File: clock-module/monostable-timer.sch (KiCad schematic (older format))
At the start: 8 parts

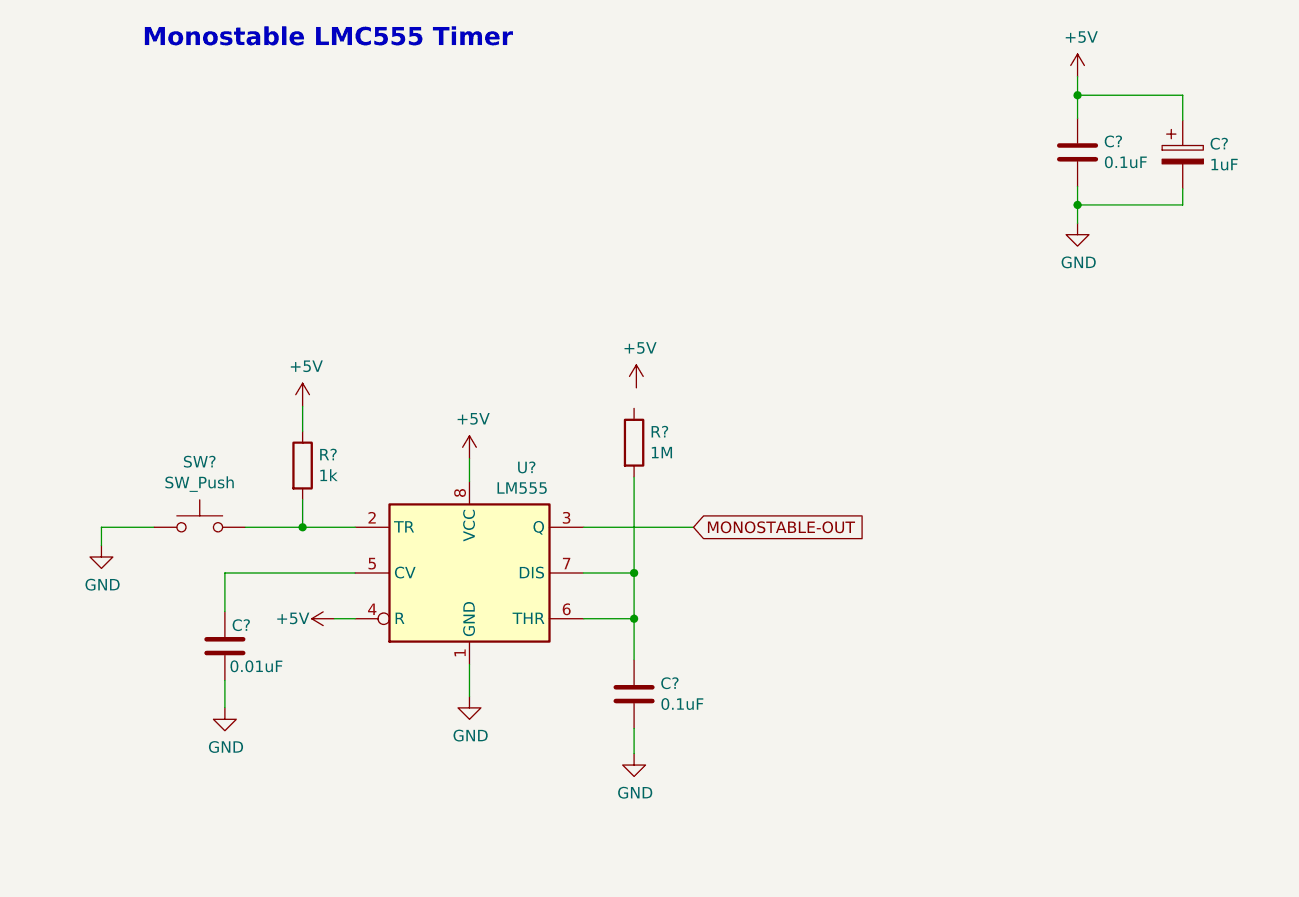
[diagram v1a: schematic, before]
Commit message: Add LED to all outputs of clocl-module
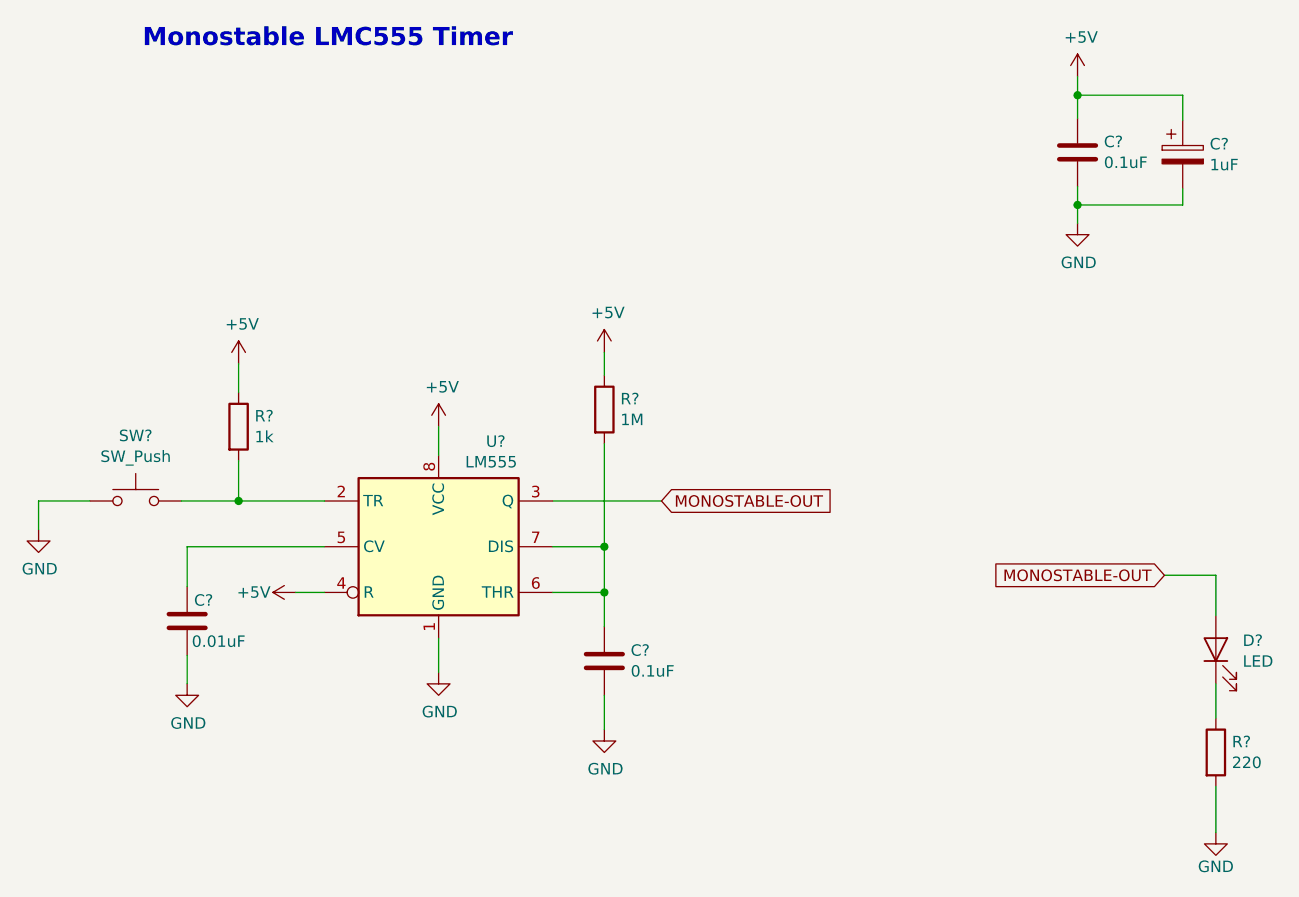
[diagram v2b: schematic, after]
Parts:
- added D?: LED, symbol Device:LED
- added R?: 220, symbol Device:R
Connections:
- net +5V: now also R?.1
- net GND: now also R?.2
- net MONOSTABLE-OUT: now also D?.2 (A)
- new net: D?.1 (K), R?.1
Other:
- moved on the sheet: C?, R?, SW?, U?

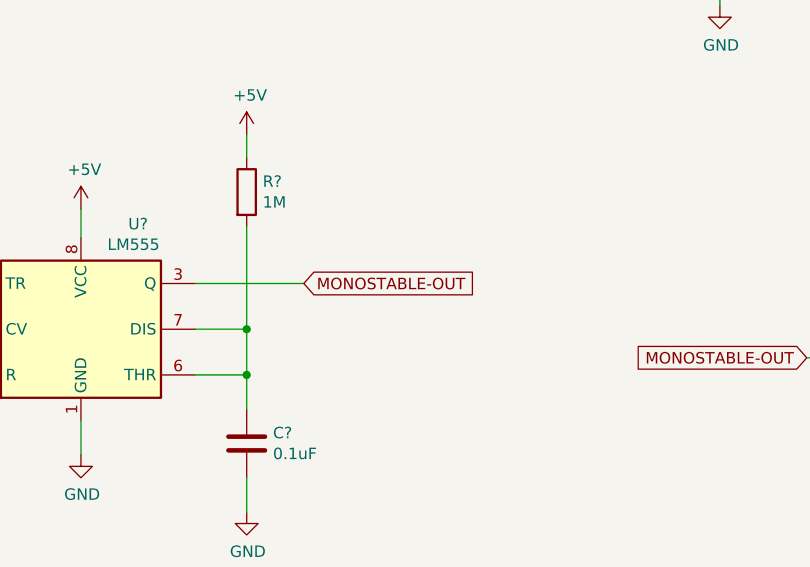
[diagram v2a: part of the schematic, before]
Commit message: Add clock inverter to clock-module, correct label directions
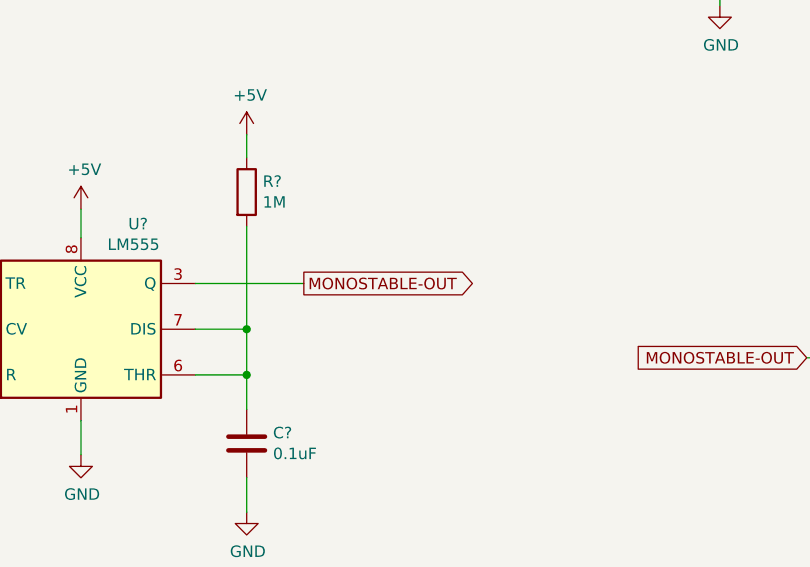
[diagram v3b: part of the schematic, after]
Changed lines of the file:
@@
 Wire Wire Line
 	9125 5075 9125 5275
-Text GLabel 6700 3825 2    50   Input ~ 0
+Text GLabel 6700 3825 2    50   Output ~ 0
 MONOSTABLE-OUT
 Wire Wire Line

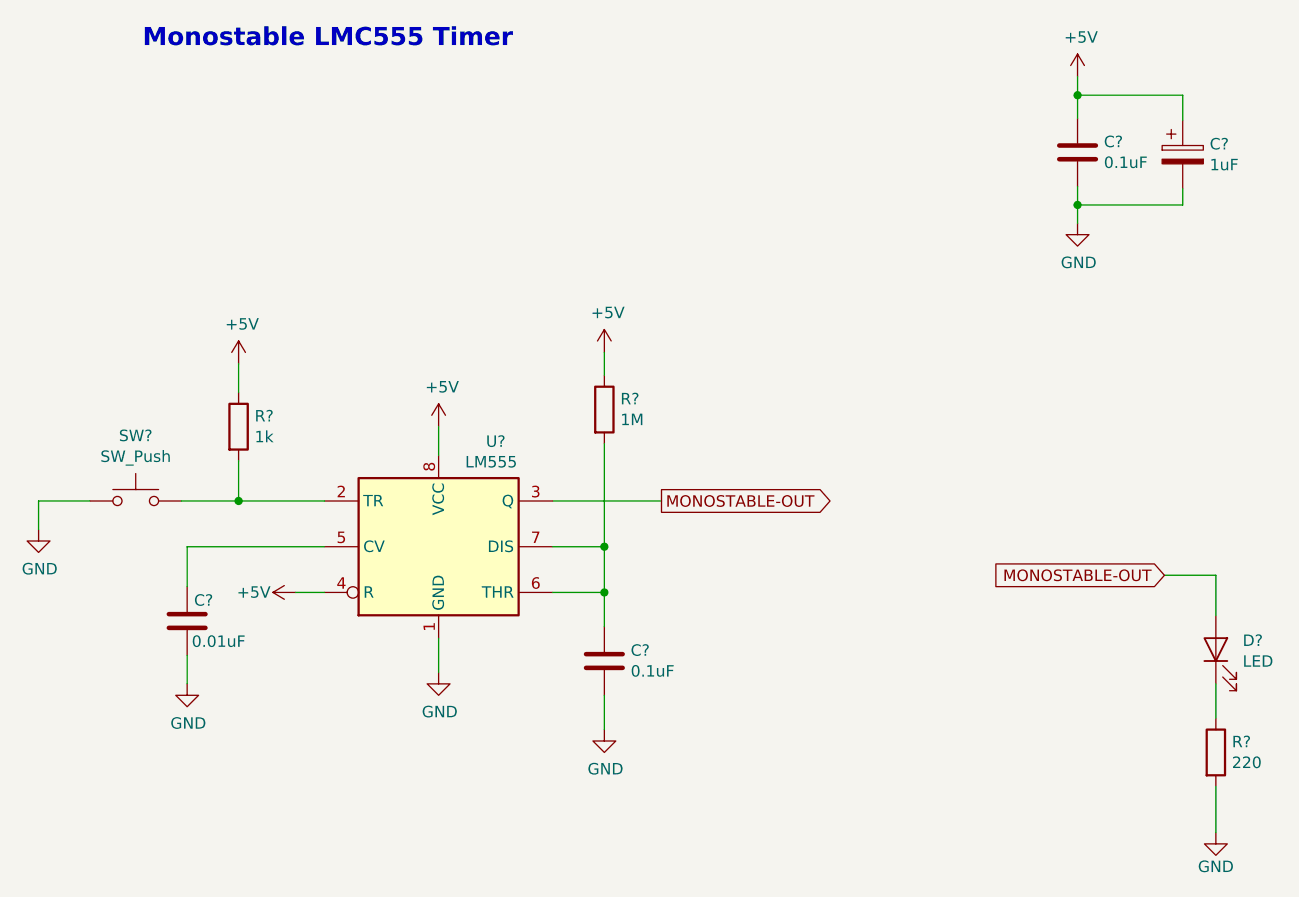
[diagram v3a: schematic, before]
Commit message: ERC complete on clock-module, add HLT connector
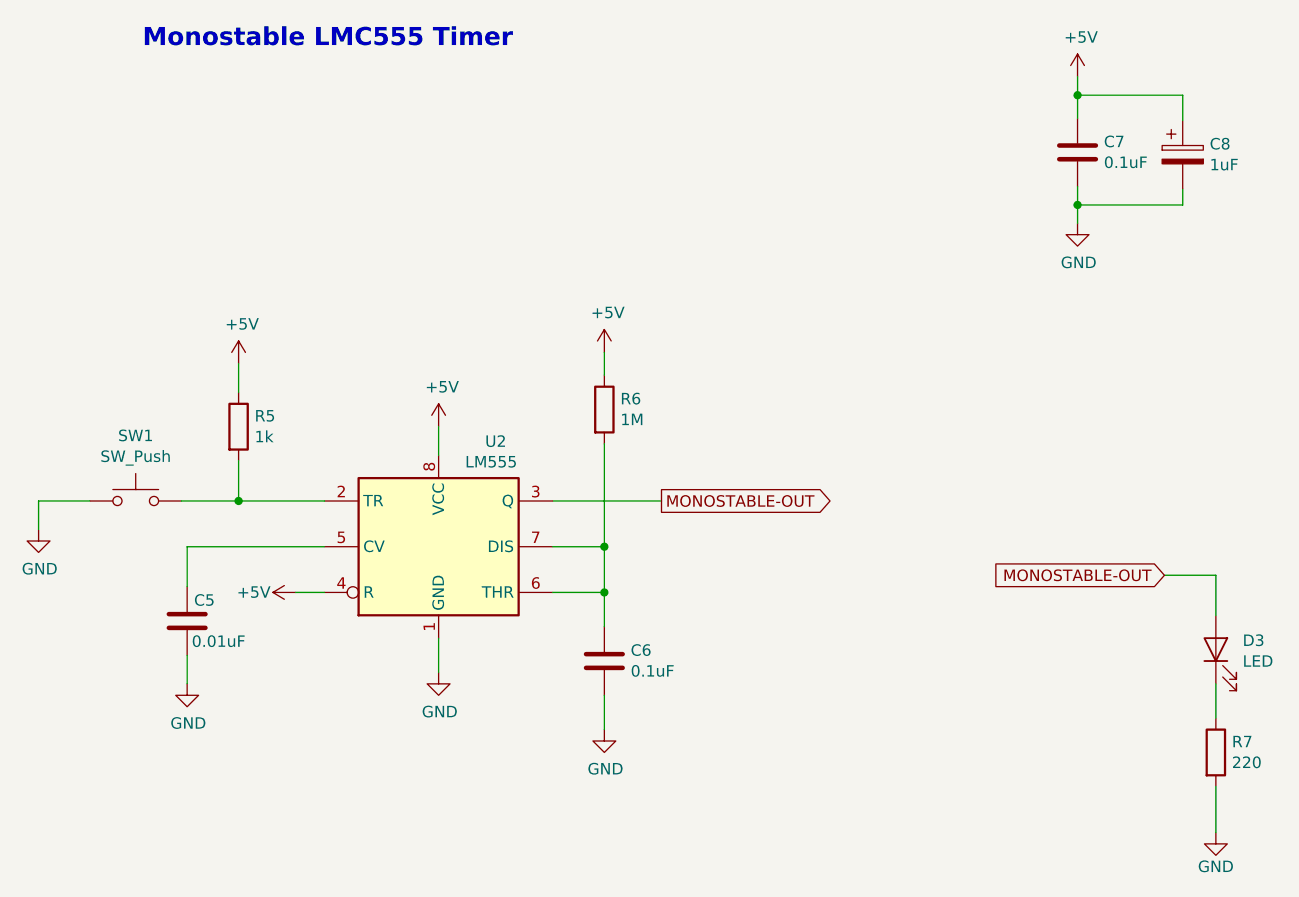
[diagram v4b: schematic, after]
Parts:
- gave numbers to parts that had none: 10
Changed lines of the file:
@@
 P 5725 4025
 AR Path="/5D27ED24" Ref="U?"  Part="1"
-AR Path="/5D26F003/5D27ED24" Ref="U?"  Part="1"
-F 0 "U?" H 5975 4485 50  0000 C CNN
+AR Path="/5D26F003/5D27ED24" Ref="U2"  Part="1"
+F 0 "U2" H 5975 4485 50  0000 C CNN
 F 1 "LM555" H 5955 4395 50  0000 C CNN
 F 2 "" H 5725 4025 50  0001 C CNN
@@
 P 4625 4350
 AR Path="/5D27ED2A" Ref="C?"  Part="1"
-AR Path="/5D26F003/5D27ED2A" Ref="C?"  Part="1"
-F 0 "C?" H 4655 4440 50  0000 L CNN
+AR Path="/5D26F003/5D27ED2A" Ref="C5"  Part="1"
+F 0 "C5" H 4655 4440 50  0000 L CNN
 F 1 "0.01uF" H 4645 4260 50  0000 L CNN
 F 2 "" H 4663 4200 50  0001 C CNN
@@
 P 8520 2300
 AR Path="/5D27ED30" Ref="C?"  Part="1"
-AR Path="/5D26F003/5D27ED30" Ref="C?"  Part="1"
-F 0 "C?" H 8635 2346 50  0000 L CNN
+AR Path="/5D26F003/5D27ED30" Ref="C7"  Part="1"
+F 0 "C7" H 8635 2346 50  0000 L CNN
 F 1 "0.1uF" H 8635 2255 50  0000 L CNN
 F 2 "" H 8558 2150 50  0001 C CNN
@@
 P 4850 3500
 AR Path="/5D27ED36" Ref="R?"  Part="1"
-AR Path="/5D26F003/5D27ED36" Ref="R?"  Part="1"
-F 0 "R?" H 4920 3546 50  0000 L CNN
+AR Path="/5D26F003/5D27ED36" Ref="R5"  Part="1"
+F 0 "R5" H 4920 3546 50  0000 L CNN
 F 1 "1k" H 4920 3455 50  0000 L CNN
 F 2 "" V 4780 3500 50  0001 C CNN
@@
 P 6450 3425
 AR Path="/5D27ED3C" Ref="R?"  Part="1"
-AR Path="/5D26F003/5D27ED3C" Ref="R?"  Part="1"
-F 0 "R?" H 6520 3471 50  0000 L CNN
+AR Path="/5D26F003/5D27ED3C" Ref="R6"  Part="1"
+F 0 "R6" H 6520 3471 50  0000 L CNN
 F 1 "1M" H 6520 3380 50  0000 L CNN
 F 2 "" V 6380 3425 50  0001 C CNN
@@
 P 4400 3825
 AR Path="/5D27ED42" Ref="SW?"  Part="1"
-AR Path="/5D26F003/5D27ED42" Ref="SW?"  Part="1"
-F 0 "SW?" H 4400 4110 50  0000 C CNN
+AR Path="/5D26F003/5D27ED42" Ref="SW1"  Part="1"
+F 0 "SW1" H 4400 4110 50  0000 C CNN
 F 1 "SW_Push" H 4400 4019 50  0000 C CNN
 F 2 "" H 4400 4025 50  0001 C CNN
@@
 Monostable LMC555 Timer
 $Comp
-L Device:CP C?
+L Device:CP C8
 U 1 1 5D27EF7E
 P 8980 2310
-F 0 "C?" H 9098 2356 50  0000 L CNN
+F 0 "C8" H 9098 2356 50  0000 L CNN
 F 1 "1uF" H 9098 2265 50  0000 L CNN
 F 2 "" H 9018 2160 50  0001 C CNN
@@
 $EndComp
 $Comp
-L power:+5V #PWR?
+L power:+5V #PWR0117
 U 1 1 5D284C5B
 P 8520 1970
-F 0 "#PWR?" H 8520 1820 50  0001 C CNN
+F 0 "#PWR0117" H 8520 1820 50  0001 C CNN
 F 1 "+5V" H 8535 2143 50  0000 C CNN
 F 2 "" H 8520 1970 50  0001 C CNN
@@
 P 6450 4525
 AR Path="/5D28683E" Ref="C?"  Part="1"
-AR Path="/5D26F003/5D28683E" Ref="C?"  Part="1"
-F 0 "C?" H 6565 4571 50  0000 L CNN
+AR Path="/5D26F003/5D28683E" Ref="C6"  Part="1"
+F 0 "C6" H 6565 4571 50  0000 L CNN
 F 1 "0.1uF" H 6565 4480 50  0000 L CNN
 F 2 "" H 6488 4375 50  0001 C CNN
@@
 $EndComp
 $Comp
-L power:+5V #PWR?
+L power:+5V #PWR0118
 U 1 1 5D28722A
 P 5725 3500
-F 0 "#PWR?" H 5725 3350 50  0001 C CNN
+F 0 "#PWR0118" H 5725 3350 50  0001 C CNN
 F 1 "+5V" H 5740 3673 50  0000 C CNN
 F 2 "" H 5725 3500 50  0001 C CNN
@@
 $EndComp
 $Comp
-L power:+5V #PWR?
+L power:+5V #PWR0119
 U 1 1 5D287ACE
 P 6450 3175
-F 0 "#PWR?" H 6450 3025 50  0001 C CNN
+F 0 "#PWR0119" H 6450 3025 50  0001 C CNN
 F 1 "+5V" H 6465 3348 50  0000 C CNN
 F 2 "" H 6450 3175 50  0001 C CNN
@@
 $EndComp
 $Comp
-L power:+5V #PWR?
+L power:+5V #PWR0120
 U 1 1 5D28807D
 P 5100 4225
-F 0 "#PWR?" H 5100 4075 50  0001 C CNN
+F 0 "#PWR0120" H 5100 4075 50  0001 C CNN
 F 1 "+5V" V 5100 4335 50  0000 L CNN
 F 2 "" H 5100 4225 50  0001 C CNN
@@
 $EndComp
 $Comp
-L power:GND #PWR?
+L power:GND #PWR0121
 U 1 1 5D28A334
 P 4625 4625
-F 0 "#PWR?" H 4625 4375 50  0001 C CNN
+F 0 "#PWR0121" H 4625 4375 50  0001 C CNN
 F 1 "GND" H 4630 4452 50  0000 C CNN
 F 2 "" H 4625 4625 50  0001 C CNN
@@
 $EndComp
 $Comp
-L power:GND #PWR?
+L power:GND #PWR0122
 U 1 1 5D28A92A
 P 6450 4825
-F 0 "#PWR?" H 6450 4575 50  0001 C CNN
+F 0 "#PWR0122" H 6450 4575 50  0001 C CNN
 F 1 "GND" H 6455 4652 50  0000 C CNN
 F 2 "" H 6450 4825 50  0001 C CNN
@@
 $EndComp
 $Comp
-L power:GND #PWR?
+L power:GND #PWR0123
 U 1 1 5D28AEA2
 P 5725 4575
-F 0 "#PWR?" H 5725 4325 50  0001 C CNN
+F 0 "#PWR0123" H 5725 4325 50  0001 C CNN
 F 1 "GND" H 5730 4402 50  0000 C CNN
 F 2 "" H 5725 4575 50  0001 C CNN
@@
 $EndComp
 $Comp
-L power:GND #PWR?
+L power:GND #PWR0124
 U 1 1 5D28D4DC
 P 3975 3950
-F 0 "#PWR?" H 3975 3700 50  0001 C CNN
+F 0 "#PWR0124" H 3975 3700 50  0001 C CNN
 F 1 "GND" H 3980 3777 50  0000 C CNN
 F 2 "" H 3975 3950 50  0001 C CNN
@@
 $EndComp
 $Comp
-L power:GND #PWR?
+L power:GND #PWR0125
 U 1 1 5D2905B3
 P 8520 2610
-F 0 "#PWR?" H 8520 2360 50  0001 C CNN
+F 0 "#PWR0125" H 8520 2360 50  0001 C CNN
 F 1 "GND" H 8525 2437 50  0000 C CNN
 F 2 "" H 8520 2610 50  0001 C CNN
@@
 	8520 2530 8520 2450
 $Comp
-L Device:LED D?
+L Device:LED D3
 U 1 1 5D29EFAA
 P 9125 4475
-F 0 "D?" V 9164 4358 50  0000 R CNN
+F 0 "D3" V 9164 4358 50  0000 R CNN
 F 1 "LED" V 9073 4358 50  0000 R CNN
 F 2 "" H 9125 4475 50  0001 C CNN
@@
 P 9125 5275
 AR Path="/5D26EDA1/5D29EFB0" Ref="#PWR?"  Part="1"
-AR Path="/5D26F003/5D29EFB0" Ref="#PWR?"  Part="1"
-F 0 "#PWR?" H 9125 5025 50  0001 C CNN
+AR Path="/5D26F003/5D29EFB0" Ref="#PWR0126"  Part="1"
+F 0 "#PWR0126" H 9125 5025 50  0001 C CNN
 F 1 "GND" H 9125 5125 50  0000 C CNN
 F 2 "" H 9125 5275 50  0001 C CNN
@@
 MONOSTABLE-OUT
 $Comp
-L Device:R R?
+L Device:R R7
 U 1 1 5D29F962
 P 9125 4925
-F 0 "R?" H 9195 4971 50  0000 L CNN
+F 0 "R7" H 9195 4971 50  0000 L CNN
 F 1 "220" H 9195 4880 50  0000 L CNN
 F 2 "" V 9055 4925 50  0001 C CNN
@@
 	6450 4675 6450 4825
 $Comp
-L power:+5V #PWR?
+L power:+5V #PWR0127
 U 1 1 5D28C940
 P 4850 3225
-F 0 "#PWR?" H 4850 3075 50  0001 C CNN
+F 0 "#PWR0127" H 4850 3075 50  0001 C CNN
 F 1 "+5V" H 4865 3398 50  0000 C CNN
 F 2 "" H 4850 3225 50  0001 C CNN
